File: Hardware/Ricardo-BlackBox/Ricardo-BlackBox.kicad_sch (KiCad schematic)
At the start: 45 parts, among them J1 RBUS, J3 Conn_02x04_Odd_Even, U1 ESP32-S3, U6 XTSD08G, U7 LM66200DRLR, Y1 R940000171

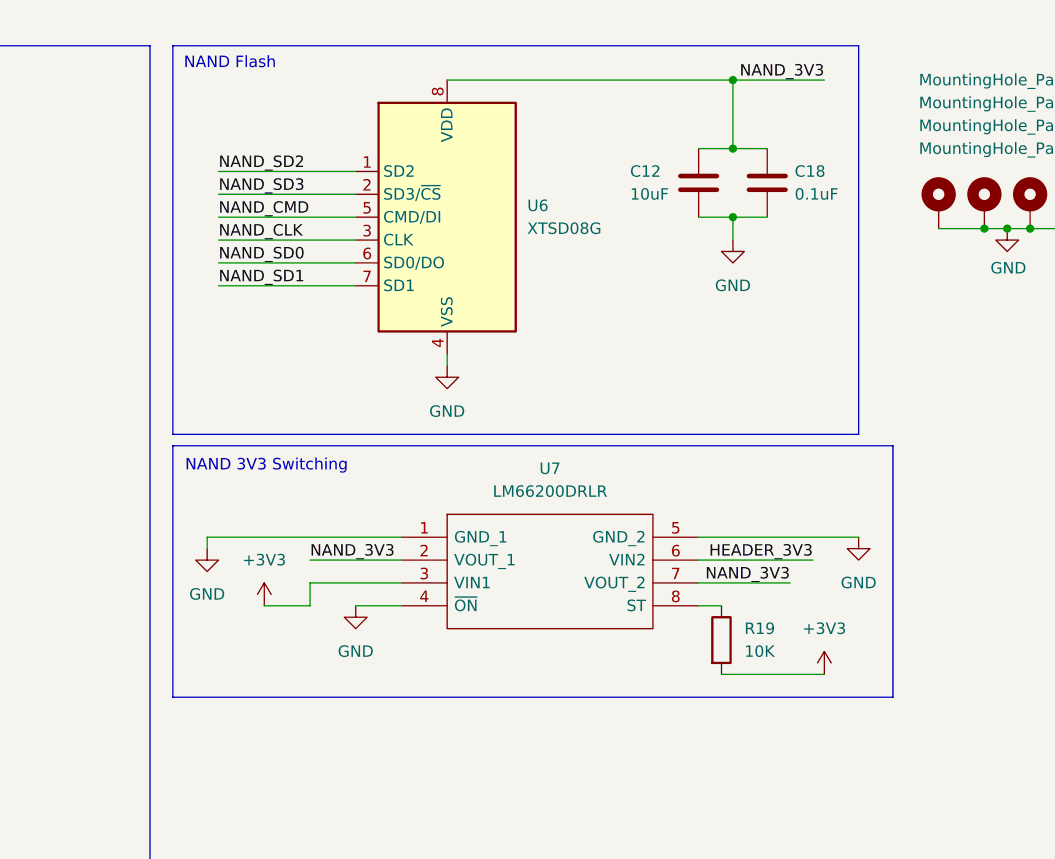
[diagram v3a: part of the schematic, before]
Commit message: Changed NAND flash to ZDSD04GLGEAG
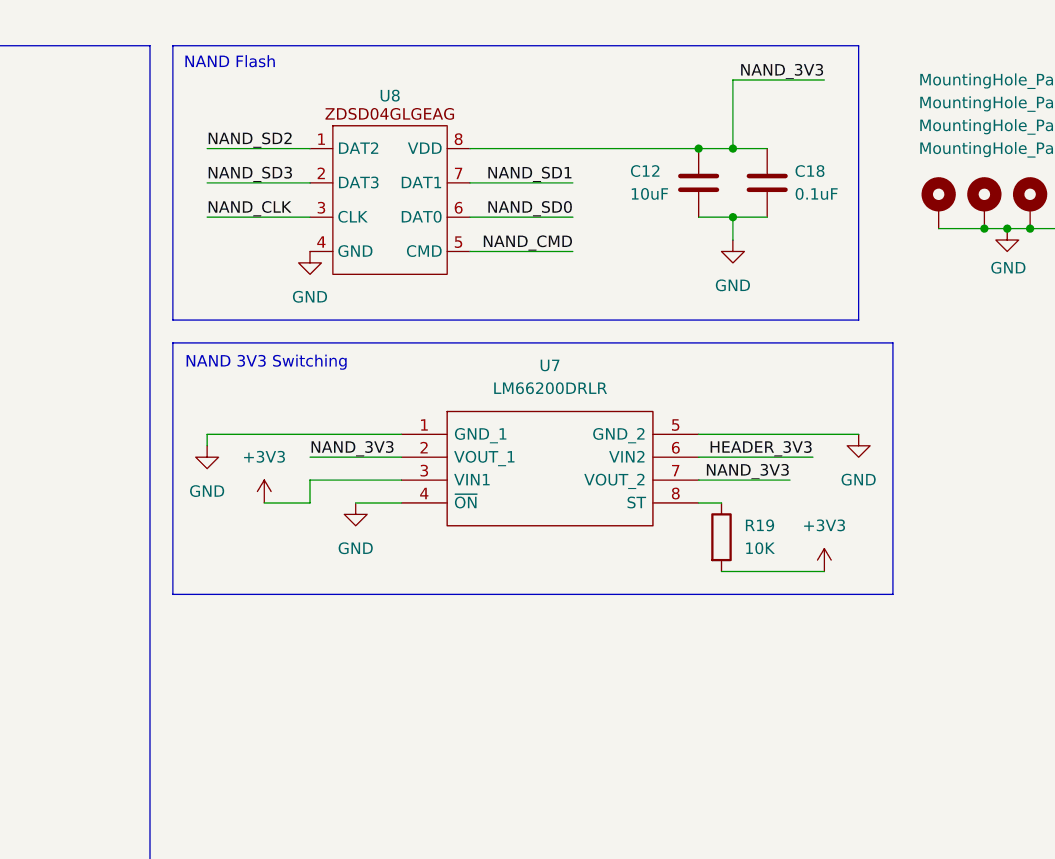
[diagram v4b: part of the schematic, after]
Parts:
- removed U6: XTSD08G, Package_LGA:LGA-8_8x6mm_P1.27mm, symbol Memory_Flash:XTSD08G
- added U8: ~, Package_LGA:LGA-8_8x6mm_P1.27mm, symbol iclr:ZDSD04GLGEAG
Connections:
- net GND: now also U8.4 (GND)
- net NAND_3V3: now also U8.8 (VDD)
- net NAND_CLK: now also U8.3 (CLK)
- net NAND_CMD: now also U8.5 (CMD)
- net NAND_SD0: now also U8.6 (DAT0)
- net NAND_SD1: now also U8.7 (DAT1)
- net NAND_SD2: now also U8.1 (DAT2)
- net NAND_SD3: now also U8.2 (DAT3)
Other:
- moved on the sheet: R19, U7

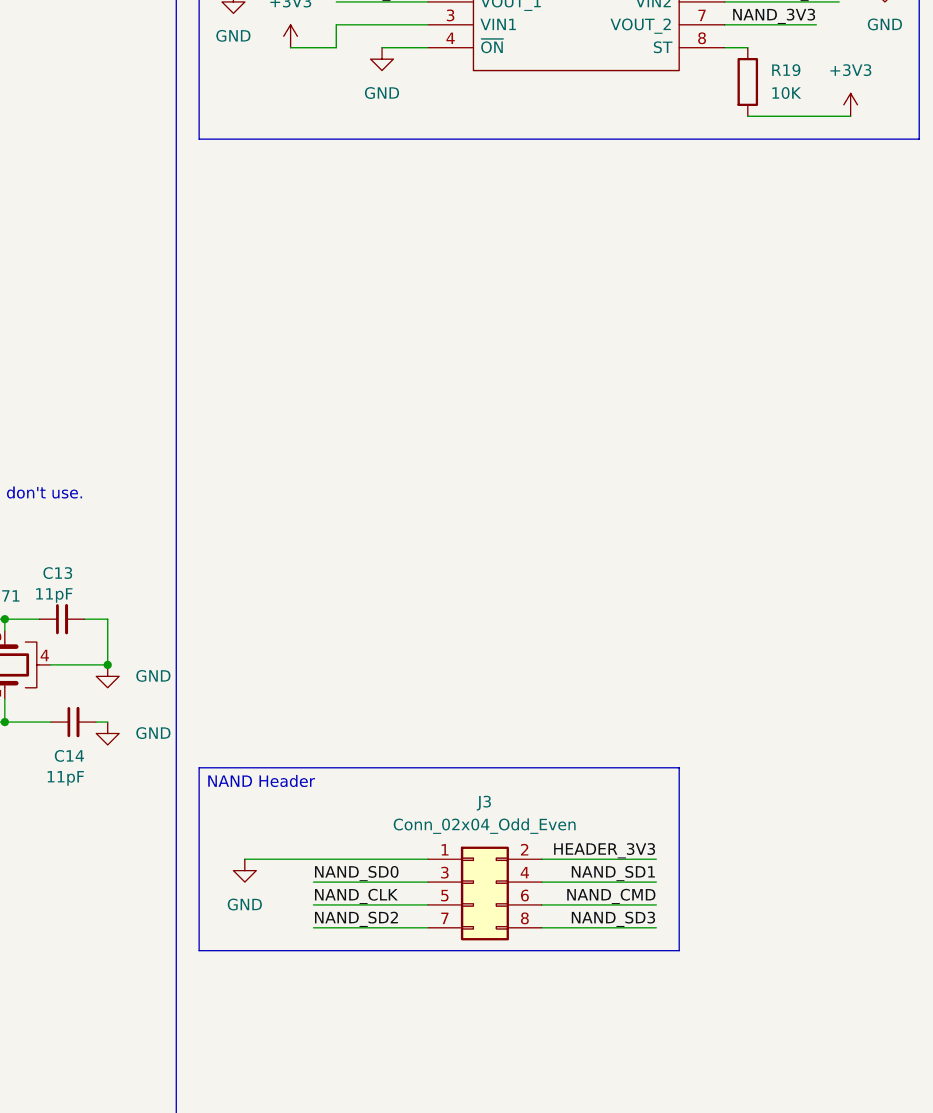
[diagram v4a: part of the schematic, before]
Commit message: Switched to PicoBlade connector
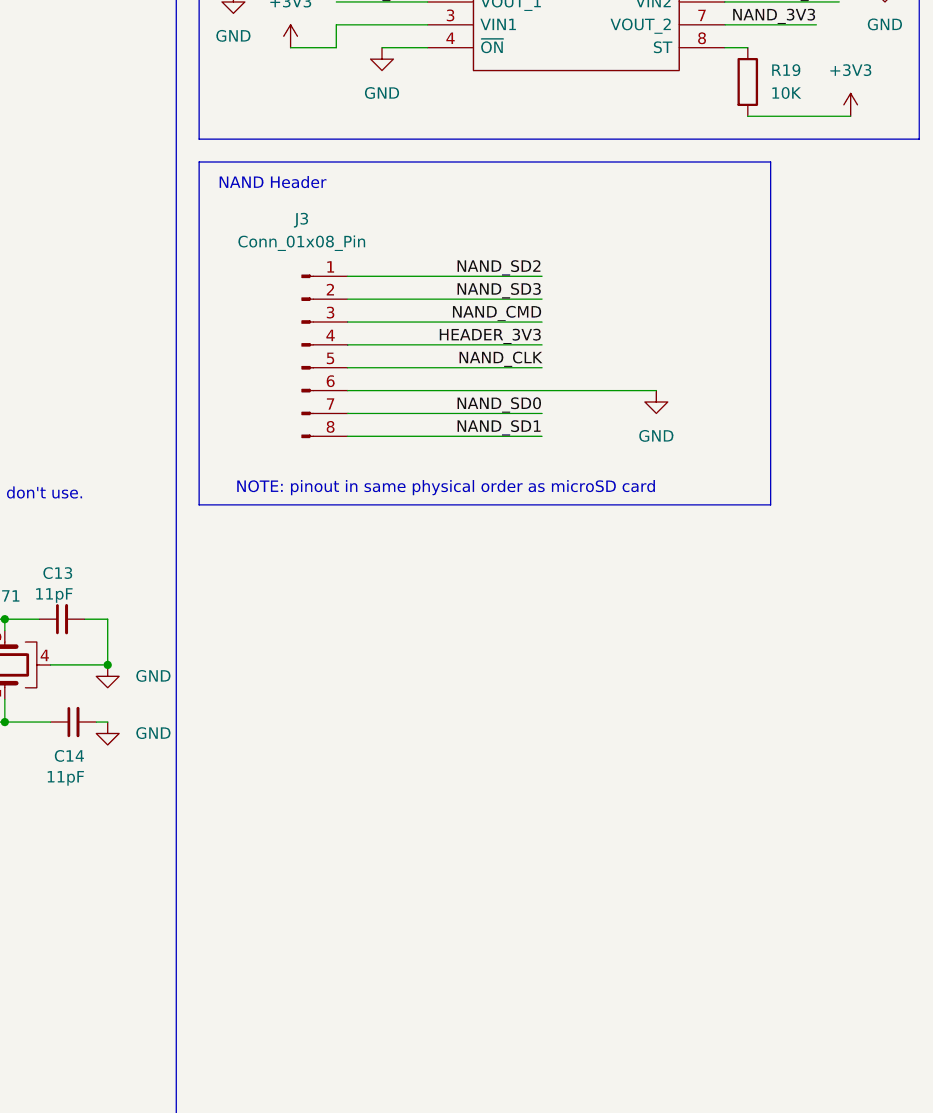
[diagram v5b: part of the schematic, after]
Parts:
- removed J3: Conn_02x04_Odd_Even, Connector_PinHeader_2.54mm:PinHeader_2x04_P2.54mm_Vertical, symbol Connector_Generic:Conn_02x04_Odd_Even
- added J3: Conn_01x08_Pin, Connector_Molex:Molex_PicoBlade_53261-0871_1x08-1MP_P1.25mm_Horizontal, symbol Connector:Conn_01x08_Pin
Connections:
- net GND: now also J3.6 (Pin_6)
- net HEADER_3V3: now also J3.4 (Pin_4)
- net NAND_CLK: now also J3.5 (Pin_5)
- net NAND_CMD: now also J3.3 (Pin_3)
- net NAND_SD0: now also J3.7 (Pin_7)
- net NAND_SD1: now also J3.8 (Pin_8)
- net NAND_SD2: now also J3.1 (Pin_1)
- net NAND_SD3: now also J3.2 (Pin_2)
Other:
- note added: "NOTE: pinout in same physical order as microSD card"

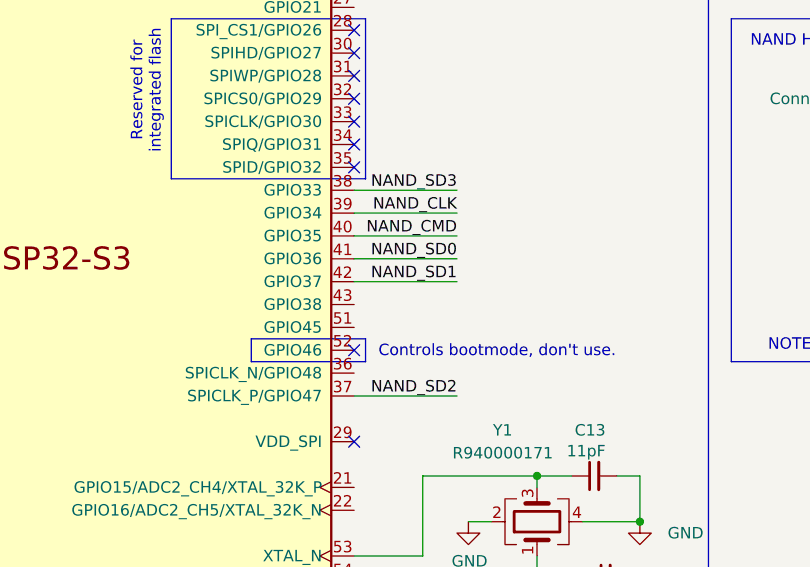
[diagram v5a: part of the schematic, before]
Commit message: Changed to PicoClasp connector
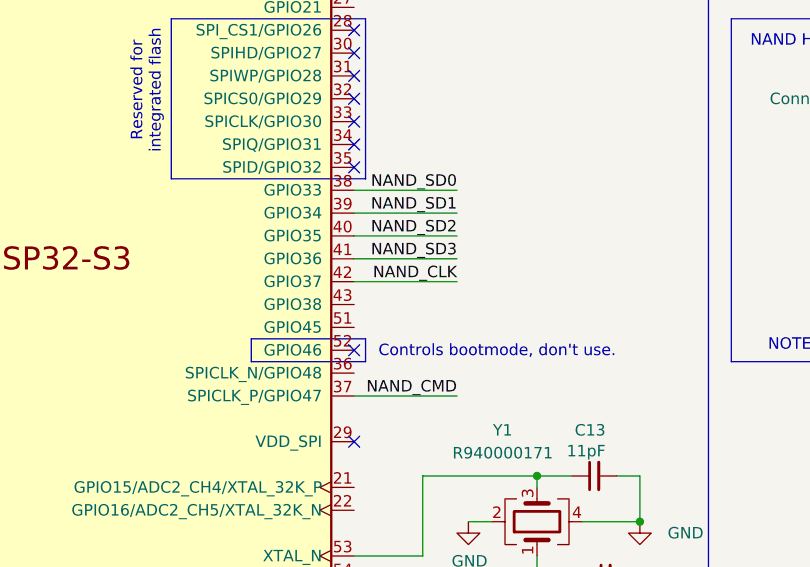
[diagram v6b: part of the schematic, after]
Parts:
- J3: footprint Connector_Molex:Molex_PicoBlade_53261-0871_1x08-1MP_P1.25mm_Horizontal -> Connector_Molex:Molex_Pico-Clasp_202396-0807_1x08-1MP_P1.00mm_Horizontal
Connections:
- net NAND_CLK: now also U1.42 (GPIO37); no longer U1.39 (GPIO34)
- net NAND_CMD: now also U1.37 (SPICLK_P/GPIO47); no longer U1.40 (GPIO35)
- net NAND_SD0: now also U1.38 (GPIO33); no longer U1.41 (GPIO36)
- net NAND_SD1: now also U1.39 (GPIO34); no longer U1.42 (GPIO37)
- net NAND_SD2: now also U1.40 (GPIO35); no longer U1.37 (SPICLK_P/GPIO47)
- net NAND_SD3: now also U1.41 (GPIO36); no longer U1.38 (GPIO33)
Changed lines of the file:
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@@
 		)
 	)
-	(label "NAND_SD3"
+	(label "NAND_SD0"
 		(at 147.32 95.25 180)
 		(fields_autoplaced yes)
@@
 		)
 	)
-	(label "NAND_SD1"
+	(label "NAND_CLK"
 		(at 147.32 105.41 180)
 		(fields_autoplaced yes)
@@
 		)
 	)
-	(label "NAND_CMD"
+	(label "NAND_SD2"
 		(at 147.32 100.33 180)
 		(fields_autoplaced yes)
@@
 		)
 	)
-	(label "NAND_SD0"
+	(label "NAND_SD3"
 		(at 147.32 102.87 180)
 		(fields_autoplaced yes)
@@
 		)
 	)
-	(label "NAND_CLK"
+	(label "NAND_SD1"
 		(at 147.32 97.79 180)
 		(fields_autoplaced yes)
@@
 		)
 	)
-	(label "NAND_SD2"
+	(label "NAND_CMD"
 		(at 147.32 118.11 180)
 		(fields_autoplaced yes)
@@
 			)
 		)
-		(property "Footprint" "Connector_Molex:Molex_PicoBlade_53261-0871_1x08-1MP_P1.25mm_Horizontal"
+		(property "Footprint" "Connector_Molex:Molex_Pico-Clasp_202396-0807_1x08-1MP_P1.00mm_Horizontal"
 			(at 189.23 96.52 0)
 			(effects
